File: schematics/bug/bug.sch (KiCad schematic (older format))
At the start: 16 parts, among them P1 CONN_01X09, P2 CONN_01X02, P3 CONN_01X06, P4 CONN_01X02, U1 uln2803A, U2 Arduino_Mini, U3 SPX2920U-3.3, U4 ESP8266, U5 button

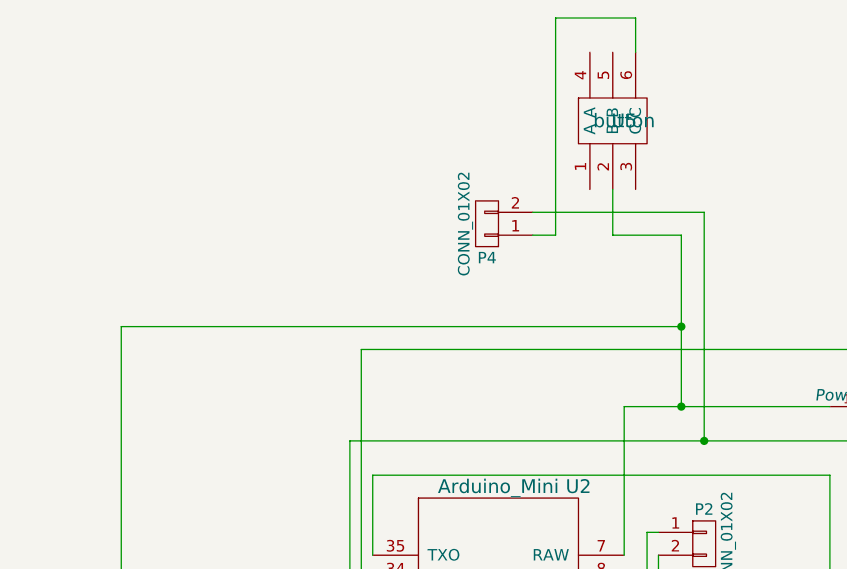
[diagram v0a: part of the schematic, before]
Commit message: Update schematic lineSensor and bug
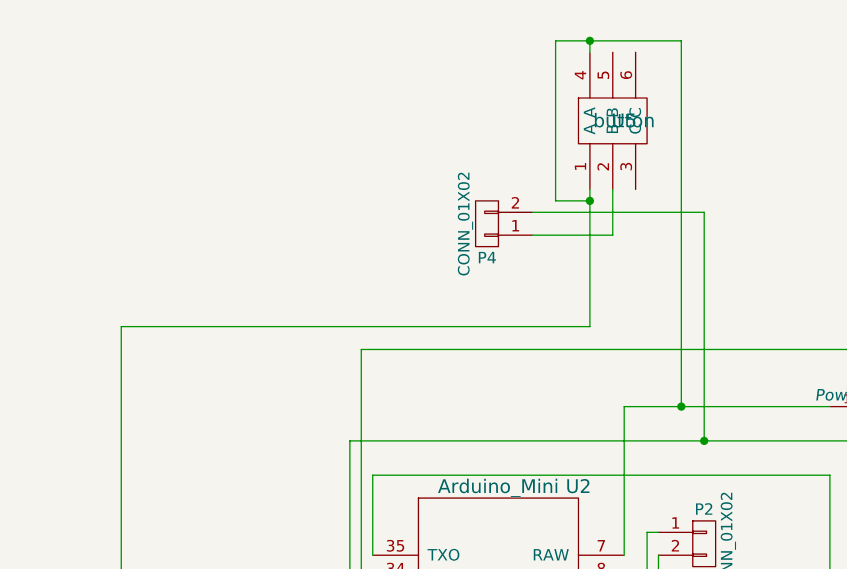
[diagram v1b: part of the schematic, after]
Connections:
- net at P1.9 (P9), U1.10 (COM), U2.7 (RAW)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: now also U5.1 (A), U5.4 (A); no longer U5.2 (B)
- net at P4.1 (P1): now also U5.2 (B); no longer U5.6 (C)
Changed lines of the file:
@@
 EESchema Schematic File Version 2
-LIBS:bug-rescue
 LIBS:power
 LIBS:device
@@
 	5400 2400 6300 2400
 Wire Wire Line
-	5650 1650 5650 2400
-Wire Wire Line
 	5500 3150 5400 3150
 Wire Wire Line
@@
 Connection ~ 7250 4850
 Wire Wire Line
-	3200 2050 5650 2050
-Connection ~ 5650 2050
-Wire Wire Line
 	3200 2050 3200 3350
 Connection ~ 3200 3350
@@
 Wire Wire Line
 	5000 1550 5750 1550
+Wire Wire Line
+	5000 1650 5350 1650
+Wire Wire Line
+	5500 2950 5500 3150
+Wire Wire Line
+	4200 2550 6400 2550
+Wire Wire Line
+	4200 3350 4200 2550
+Connection ~ 5750 2550
+Connection ~ 4200 3350
+Wire Wire Line
+	5350 1650 5350 1450
+Wire Wire Line
+	3200 2050 5250 2050
+Wire Wire Line
+	5250 2050 5250 1450
+Wire Wire Line
+	5100 800  5650 800
+Wire Wire Line
+	5650 800  5650 2400
 $Comp
 L button U5
@@
 $EndComp
 Wire Wire Line
-	5650 1650 5350 1650
-Wire Wire Line
-	5350 1650 5350 1450
-Wire Wire Line
-	5100 1650 5100 700
-Wire Wire Line
-	5100 700  5450 700
-Wire Wire Line
-	5450 700  5450 850
-Wire Wire Line
-	5100 1650 5000 1650
-Wire Wire Line
-	5500 2950 5500 3150
-Wire Wire Line
-	4200 2550 6400 2550
-Wire Wire Line
-	4200 3350 4200 2550
-Connection ~ 5750 2550
-Connection ~ 4200 3350
+	5250 800  5250 850
+Wire Wire Line
+	5250 1500 5100 1500
+Wire Wire Line
+	5100 1500 5100 800
+Connection ~ 5250 800
+Connection ~ 5250 1500
 $EndSCHEMATC

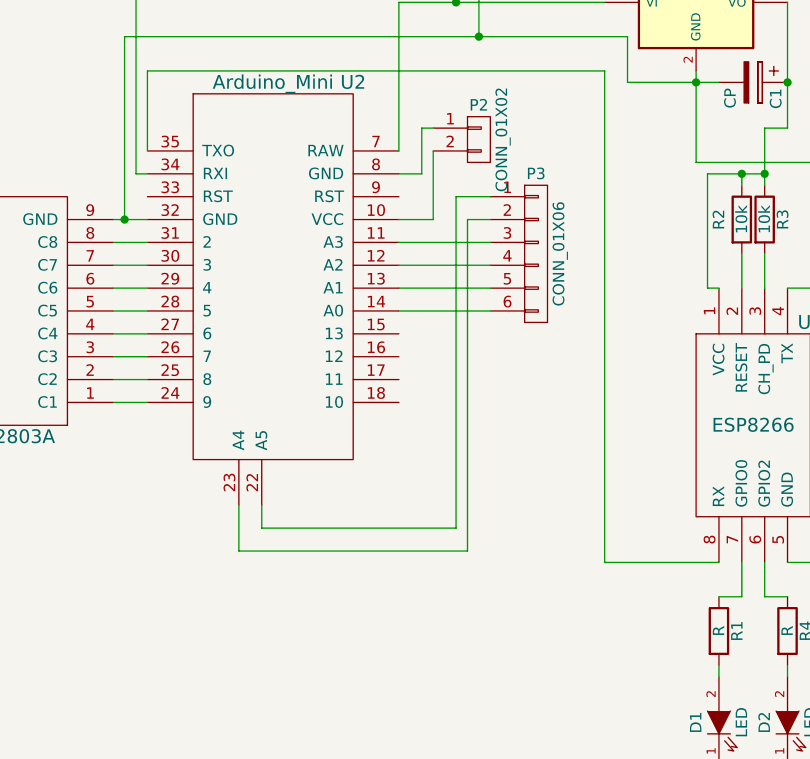
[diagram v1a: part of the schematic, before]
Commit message: SCHEMATIC: move button and led to one place
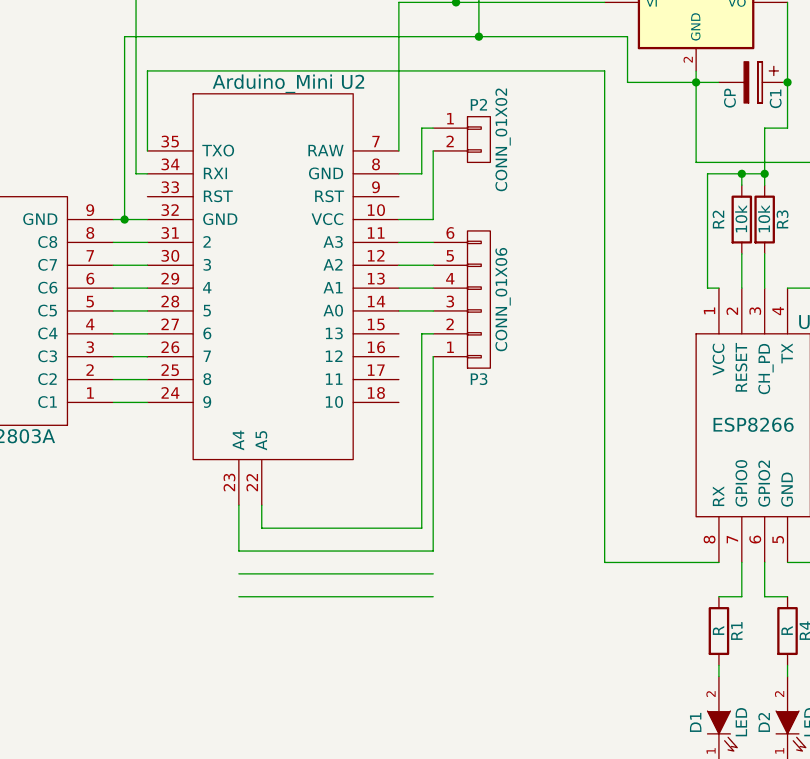
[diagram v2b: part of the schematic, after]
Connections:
- wire segments 83 -> 84
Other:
- moved on the sheet: P3
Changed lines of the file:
@@
 L CONN_01X06 P3
 U 1 1 56F1BCB1
-P 6000 3500
-F 0 "P3" H 6000 3850 50  0000 C CNN
-F 1 "CONN_01X06" V 6100 3500 50  0000 C CNN
-F 2 "Pin_Headers:Pin_Header_Straight_1x06" H 6000 3500 50  0001 C CNN
-F 3 "" H 6000 3500 50  0000 C CNN
-	1    6000 3500
-	1    0    0    -1
+P 5750 3700
+F 0 "P3" H 5750 4050 50  0000 C CNN
+F 1 "CONN_01X06" V 5850 3700 50  0000 C CNN
+F 2 "Pin_Headers:Pin_Header_Straight_1x06" H 5750 3700 50  0001 C CNN
+F 3 "" H 5750 3700 50  0000 C CNN
+	1    5750 3700
+	1    0    0    1
 $EndComp
 $Comp
@@
 	1    0    0    -1
 $EndComp
-Wire Wire Line
-	7250 3650 7100 3650
-Wire Wire Line
-	4300 3850 4150 3850
-Wire Wire Line
-	4150 3950 4300 3950
-Wire Wire Line
-	4300 4150 4150 4150
-Connection ~ 6900 3150
-Wire Wire Line
-	6750 3650 6800 3650
-Wire Wire Line
-	6750 3150 6750 3650
-Connection ~ 7000 3150
-Wire Wire Line
-	6900 3150 6900 3200
-Wire Wire Line
-	6750 3150 7000 3150
-Connection ~ 7100 2750
-Wire Wire Line
-	7000 2950 7000 3200
-Wire Wire Line
-	7100 2950 7000 2950
-Wire Wire Line
-	7100 2400 7100 2950
-Wire Wire Line
-	6400 2750 6800 2750
-Wire Wire Line
-	6700 2700 6700 3100
-Wire Wire Line
-	6400 2550 6400 2750
-Wire Wire Line
-	5750 1550 5750 2550
-Connection ~ 5650 2400
-Wire Wire Line
-	5400 2400 5400 3050
-Wire Wire Line
-	5400 2400 6300 2400
-Wire Wire Line
-	5500 3150 5400 3150
-Wire Wire Line
-	5550 2950 5500 2950
-Wire Wire Line
-	5550 3350 5400 3350
-Wire Wire Line
-	5550 3050 5550 3350
-Wire Wire Line
-	5650 3250 5800 3250
-Wire Wire Line
-	5650 4700 5650 3250
-Wire Wire Line
-	5700 3350 5700 4800
-Wire Wire Line
-	5800 3350 5700 3350
-Wire Wire Line
-	5700 4800 4700 4800
-Wire Wire Line
-	4700 4800 4700 4600
-Wire Wire Line
-	4800 4700 5650 4700
-Wire Wire Line
-	4800 4600 4800 4700
-Wire Wire Line
-	5400 3450 5800 3450
-Wire Wire Line
-	5400 3550 5800 3550
-Wire Wire Line
-	5400 3650 5800 3650
-Wire Wire Line
-	5400 3750 5800 3750
-Wire Wire Line
-	3100 3350 3250 3350
-Wire Wire Line
-	3100 3450 3250 3450
-Wire Wire Line
-	3250 3550 3100 3550
-Wire Wire Line
-	3100 3650 3250 3650
-Wire Wire Line
-	3250 3750 3100 3750
-Wire Wire Line
-	3100 3850 3250 3850
-Wire Wire Line
-	3250 3950 3100 3950
-Wire Wire Line
-	3100 4050 3250 4050
-Wire Wire Line
-	3250 4150 3100 4150
-Wire Wire Line
-	4300 4050 4150 4050
-Wire Wire Line
-	4150 3750 4300 3750
-Wire Wire Line
-	4300 3650 4150 3650
-Wire Wire Line
-	4150 3550 4300 3550
-Wire Wire Line
-	4300 3450 4150 3450
-Wire Wire Line
-	7250 5750 6800 5750
-Wire Wire Line
-	6900 3500 6900 3650
-Wire Wire Line
-	7000 3500 7000 3650
-Connection ~ 6800 5750
-Connection ~ 7100 5750
-Wire Wire Line
-	7250 4850 7250 5750
-Wire Wire Line
-	7100 4850 7350 4850
-Wire Wire Line
-	6800 5300 6800 5350
-Wire Wire Line
-	7100 5350 7100 5300
-Wire Wire Line
-	6900 5000 6800 5000
-Wire Wire Line
-	6900 4850 6900 5000
-Wire Wire Line
-	7000 5000 7000 4850
-Wire Wire Line
-	7100 5000 7000 5000
-Wire Wire Line
-	7350 4850 7350 3100
-Wire Wire Line
-	7350 3100 6700 3100
-Connection ~ 6700 2750
-Connection ~ 7250 4850
-Wire Wire Line
-	3200 2050 3200 3350
-Connection ~ 3200 3350
-Wire Wire Line
-	4150 3350 4300 3350
-Wire Wire Line
-	7250 3650 7250 2150
-Wire Wire Line
-	7250 2150 4250 2150
-Wire Wire Line
-	4250 2150 4250 3150
-Wire Wire Line
-	4250 3150 4300 3150
-Wire Wire Line
-	4300 3050 4300 2700
-Wire Wire Line
-	4300 2700 6300 2700
-Wire Wire Line
-	6300 2700 6300 4850
-Wire Wire Line
-	6300 4850 6800 4850
-Wire Wire Line
-	5000 1550 5750 1550
-Wire Wire Line
-	5000 1650 5350 1650
-Wire Wire Line
-	5500 2950 5500 3150
-Wire Wire Line
-	4200 2550 6400 2550
-Wire Wire Line
-	4200 3350 4200 2550
-Connection ~ 5750 2550
-Connection ~ 4200 3350
-Wire Wire Line
-	5350 1650 5350 1450
-Wire Wire Line
-	3200 2050 5250 2050
-Wire Wire Line
-	5250 2050 5250 1450
-Wire Wire Line
-	5100 800  5650 800
-Wire Wire Line
-	5650 800  5650 2400
 $Comp
 L button U5
@@
 $EndComp
 Wire Wire Line
+	7250 3650 7100 3650
+Wire Wire Line
+	4300 3850 4150 3850
+Wire Wire Line
+	4150 3950 4300 3950
+Wire Wire Line
+	4300 4150 4150 4150
+Connection ~ 6900 3150
+Wire Wire Line
+	6750 3650 6800 3650
+Wire Wire Line
+	6750 3150 6750 3650
+Connection ~ 7000 3150
+Wire Wire Line
+	6900 3150 6900 3200
+Wire Wire Line
+	6750 3150 7000 3150
+Connection ~ 7100 2750
+Wire Wire Line
+	7000 2950 7000 3200
+Wire Wire Line
+	7100 2950 7000 2950
+Wire Wire Line
+	7100 2400 7100 2950
+Wire Wire Line
+	6400 2750 6800 2750
+Wire Wire Line
+	6700 2700 6700 3100
+Wire Wire Line
+	6400 2550 6400 2750
+Wire Wire Line
+	5750 1550 5750 2550
+Connection ~ 5650 2400
+Wire Wire Line
+	5400 2400 5400 3050
+Wire Wire Line
+	5400 2400 6300 2400
+Wire Wire Line
+	5500 3150 5400 3150
+Wire Wire Line
+	5550 2950 5500 2950
+Wire Wire Line
+	5550 3350 5400 3350
+Wire Wire Line
+	5550 3050 5550 3350
+Wire Wire Line
+	4700 4800 4700 4600
+Wire Wire Line
+	4800 4600 4800 4700
+Wire Wire Line
+	3100 3350 3250 3350
+Wire Wire Line
+	3100 3450 3250 3450
+Wire Wire Line
+	3250 3550 3100 3550
+Wire Wire Line
+	3100 3650 3250 3650
+Wire Wire Line
+	3250 3750 3100 3750
+Wire Wire Line
+	3100 3850 3250 3850
+Wire Wire Line
+	3250 3950 3100 3950
+Wire Wire Line
+	3100 4050 3250 4050
+Wire Wire Line
+	3250 4150 3100 4150
+Wire Wire Line
+	4300 4050 4150 4050
+Wire Wire Line
+	4150 3750 4300 3750
+Wire Wire Line
+	4300 3650 4150 3650
+Wire Wire Line
+	4150 3550 4300 3550
+Wire Wire Line
+	4300 3450 4150 3450
+Wire Wire Line
+	7250 5750 6800 5750
+Wire Wire Line
+	6900 3500 6900 3650
+Wire Wire Line
+	7000 3500 7000 3650
+Connection ~ 6800 5750
+Connection ~ 7100 5750
+Wire Wire Line
+	7250 4850 7250 5750
+Wire Wire Line
+	7100 4850 7350 4850
+Wire Wire Line
+	6800 5300 6800 5350
+Wire Wire Line
+	7100 5350 7100 5300
+Wire Wire Line
+	6900 5000 6800 5000
+Wire Wire Line
+	6900 4850 6900 5000
+Wire Wire Line
+	7000 5000 7000 4850
+Wire Wire Line
+	7100 5000 7000 5000
+Wire Wire Line
+	7350 4850 7350 3100
+Wire Wire Line
+	7350 3100 6700 3100
+Connection ~ 6700 2750
+Connection ~ 7250 4850
+Wire Wire Line
+	3200 2050 3200 3350
+Connection ~ 3200 3350
+Wire Wire Line
+	4150 3350 4300 3350
+Wire Wire Line
+	7250 3650 7250 2150
+Wire Wire Line
+	7250 2150 4250 2150
+Wire Wire Line
+	4250 2150 4250 3150
+Wire Wire Line
+	4250 3150 4300 3150
+Wire Wire Line
+	4300 3050 4300 2700
+Wire Wire Line
+	4300 2700 6300 2700
+Wire Wire Line
+	6300 2700 6300 4850
+Wire Wire Line
+	6300 4850 6800 4850
+Wire Wire Line
+	5000 1550 5750 1550
+Wire Wire Line
+	5000 1650 5350 1650
+Wire Wire Line
+	5500 2950 5500 3150
+Wire Wire Line
+	4200 2550 6400 2550
+Wire Wire Line
+	4200 3350 4200 2550
+Connection ~ 5750 2550
+Connection ~ 4200 3350
+Wire Wire Line
+	5350 1650 5350 1450
+Wire Wire Line
+	3200 2050 5250 2050
+Wire Wire Line
+	5250 2050 5250 1450
+Wire Wire Line
+	5100 800  5650 800
+Wire Wire Line
+	5650 800  5650 2400
+Wire Wire Line
 	5250 800  5250 850
 Wire Wire Line
@@
 Connection ~ 5250 800
 Connection ~ 5250 1500
+Wire Wire Line
+	5400 3450 5550 3450
+Wire Wire Line
+	5400 3550 5550 3550
+Wire Wire Line
+	5400 3650 5550 3650
+Wire Wire Line
+	5400 3750 5550 3750
+Wire Wire Line
+	5550 3950 5550 4800
+Wire Wire Line
+	5550 4800 4700 4800
+Wire Wire Line
+	5550 4900 4700 4900
+Wire Wire Line
+	5550 5000 4700 5000
+Wire Wire Line
+	4800 4700 5500 4700
+Wire Wire Line
+	5500 4700 5500 3850
+Wire Wire Line
+	5500 3850 5550 3850
 $EndSCHEMATC

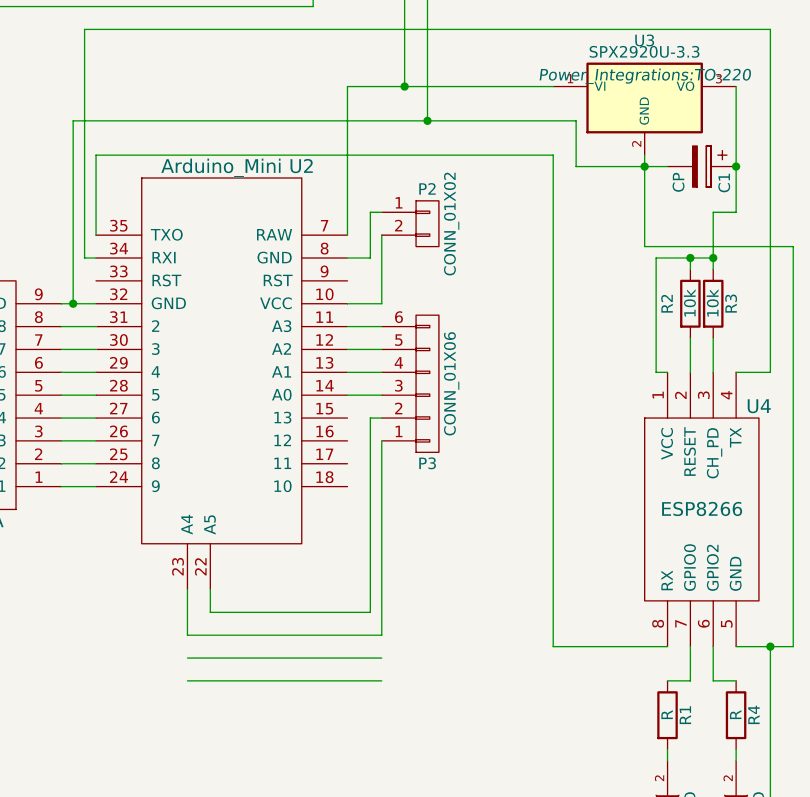
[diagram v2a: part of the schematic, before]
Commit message: SCHEMATIC: update lineSensors and bug
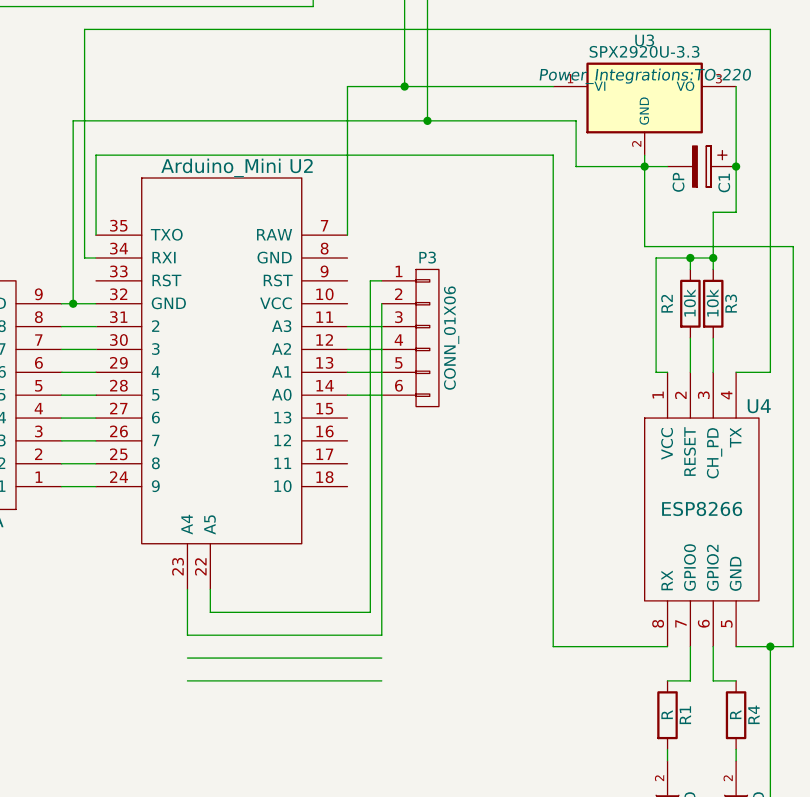
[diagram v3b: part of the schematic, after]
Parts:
- removed P2: CONN_01X02, Pin_Headers:Pin_Header_Straight_1x02, symbol CONN_01X02
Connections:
- wire segments 84 -> 79
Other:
- moved on the sheet: P3
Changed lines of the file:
@@
 L CONN_01X06 P3
 U 1 1 56F1BCB1
-P 5750 3700
-F 0 "P3" H 5750 4050 50  0000 C CNN
-F 1 "CONN_01X06" V 5850 3700 50  0000 C CNN
-F 2 "Pin_Headers:Pin_Header_Straight_1x06" H 5750 3700 50  0001 C CNN
-F 3 "" H 5750 3700 50  0000 C CNN
-	1    5750 3700
-	1    0    0    1
-$EndComp
-$Comp
-L CONN_01X02 P2
-U 1 1 56F1C32B
-P 5750 3000
-F 0 "P2" H 5750 3150 50  0000 C CNN
-F 1 "CONN_01X02" V 5850 3000 50  0000 C CNN
-F 2 "Pin_Headers:Pin_Header_Straight_1x02" H 5750 3000 50  0001 C CNN
-F 3 "" H 5750 3000 50  0000 C CNN
-	1    5750 3000
+P 5750 3500
+F 0 "P3" H 5750 3850 50  0000 C CNN
+F 1 "CONN_01X06" V 5850 3500 50  0000 C CNN
+F 2 "Pin_Headers:Pin_Header_Straight_1x06" H 5750 3500 50  0001 C CNN
+F 3 "" H 5750 3500 50  0000 C CNN
+	1    5750 3500
 	1    0    0    -1
 $EndComp
@@
 	5400 2400 6300 2400
 Wire Wire Line
-	5500 3150 5400 3150
-Wire Wire Line
-	5550 2950 5500 2950
-Wire Wire Line
-	5550 3350 5400 3350
-Wire Wire Line
-	5550 3050 5550 3350
-Wire Wire Line
 	4700 4800 4700 4600
 Wire Wire Line
@@
 	5000 1650 5350 1650
 Wire Wire Line
-	5500 2950 5500 3150
-Wire Wire Line
 	4200 2550 6400 2550
 Wire Wire Line
@@
 	5400 3750 5550 3750
 Wire Wire Line
-	5550 3950 5550 4800
-Wire Wire Line
 	5550 4800 4700 4800
 Wire Wire Line
@@
 	4800 4700 5500 4700
 Wire Wire Line
-	5500 4700 5500 3850
-Wire Wire Line
-	5500 3850 5550 3850
+	5500 4700 5500 3250
+Wire Wire Line
+	5500 3250 5550 3250
+Wire Wire Line
+	5550 3350 5550 4800
 $EndSCHEMATC

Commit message: Cleanup repository
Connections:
- wire segments 79 -> 77
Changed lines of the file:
@@
 	5550 4800 4700 4800
-Wire Wire Line
-	5550 4900 4700 4900
-Wire Wire Line
-	5550 5000 4700 5000
 Wire Wire Line
 	4800 4700 5500 4700
